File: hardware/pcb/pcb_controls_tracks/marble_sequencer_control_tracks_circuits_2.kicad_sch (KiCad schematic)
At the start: 43 parts, among them J1 Conn_01x02_Power_Supply, J2 Conn_01x02_I2C, SW1 SW_Push, SW10 SW_Push, SW11 SW_Push, SW12 SW_Push, SW13 SW_Push, SW14 SW_Push, SW15 SW_Push, SW16 SW_Push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

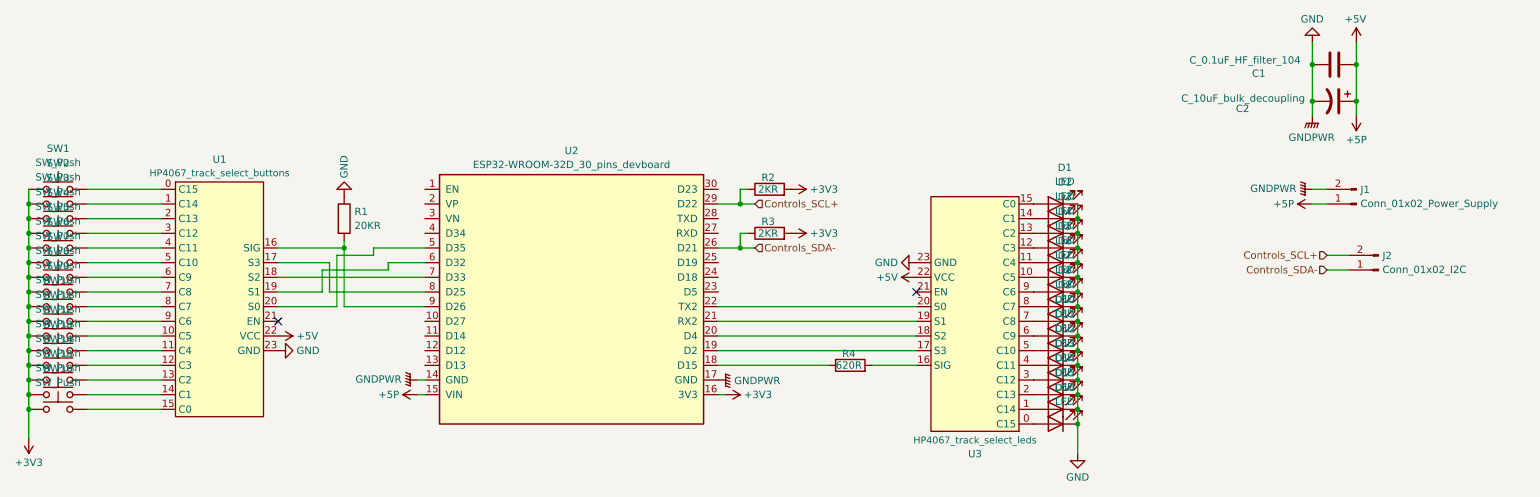
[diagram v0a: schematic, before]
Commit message: Delete solidworks temp files.
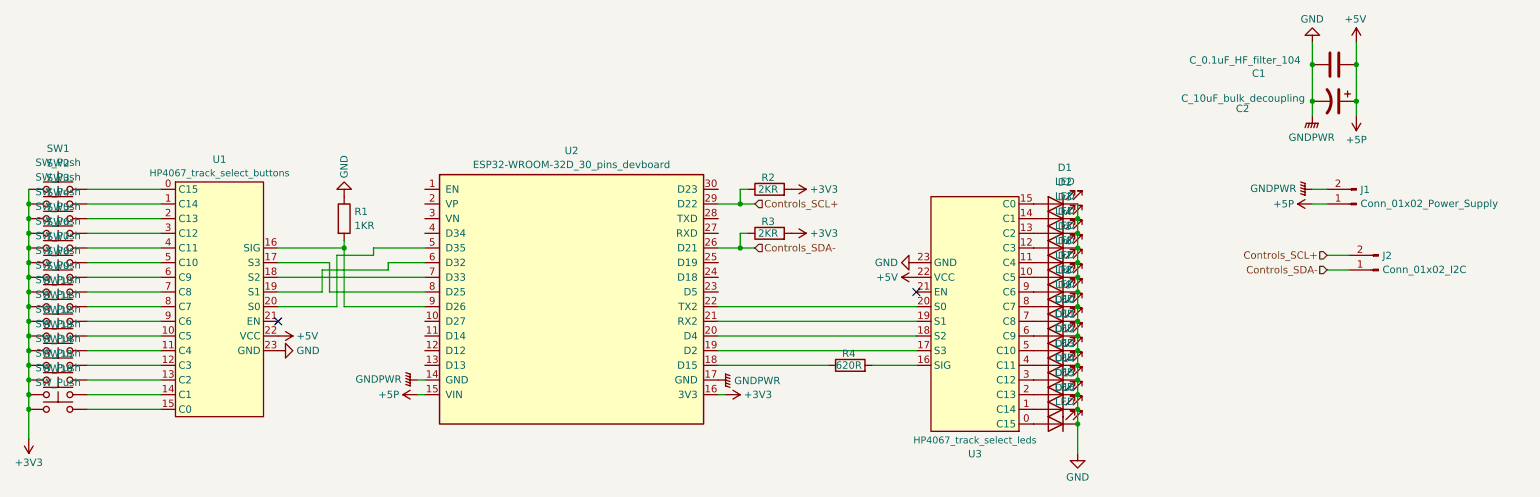
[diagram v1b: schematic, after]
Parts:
- R1: value 20KR -> 1KR
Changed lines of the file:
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@@
 (kicad_sch
-	(version 20231120)
+	(version 20250114)
 	(generator "eeschema")
-	(generator_version "8.0")
+	(generator_version "9.0")
 	(paper "A4")
 	(junction
@@
 		(shape input)
 		(at 154.94 62.23 0)
-		(fields_autoplaced yes)
 		(effects
 			(font
@@
 		(shape input)
 		(at 254 73.66 180)
-		(fields_autoplaced yes)
 		(effects
 			(font
@@
 		(shape input)
 		(at 254 71.12 180)
-		(fields_autoplaced yes)
 		(effects
 			(font
@@
 		(shape input)
 		(at 154.94 69.85 0)
-		(fields_autoplaced yes)
 		(effects
 			(font
@@
 			)
 		)
-		(property "Value" "20KR"
+		(property "Value" "1KR"
 			(at 85.598 65.9821 0)
 			(effects
@@
 		)
 	)
+	(embedded_fonts no)
 )
